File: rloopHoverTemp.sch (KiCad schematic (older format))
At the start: 23 parts, among them P1 CONN_01X01, P2 CONN_01X01, P3 CONN_01X01, P4 CONN_01X01, U1 P82B715TD, U2 MLX90614, U3 Regulator, U4 Regulator, X1 RJ45-SHIELDED, X2 RJ45-SHIELDED

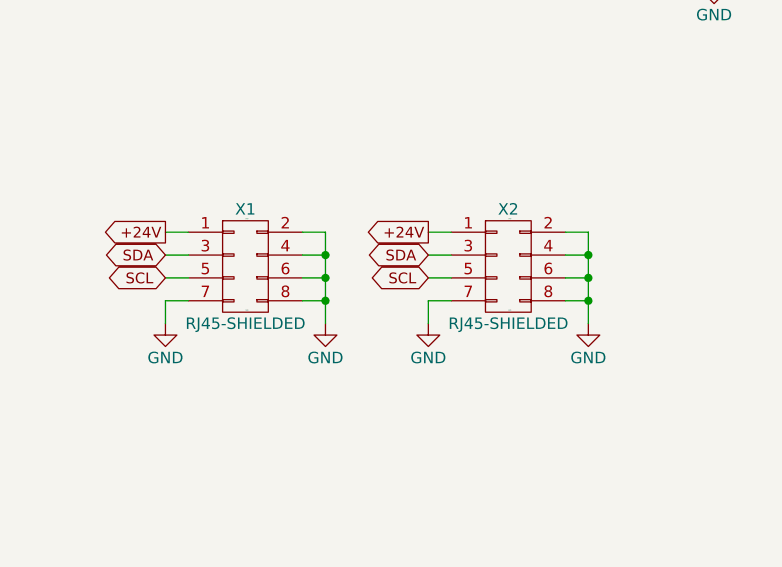
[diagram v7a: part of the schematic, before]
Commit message: different shielding scheme for RJ45
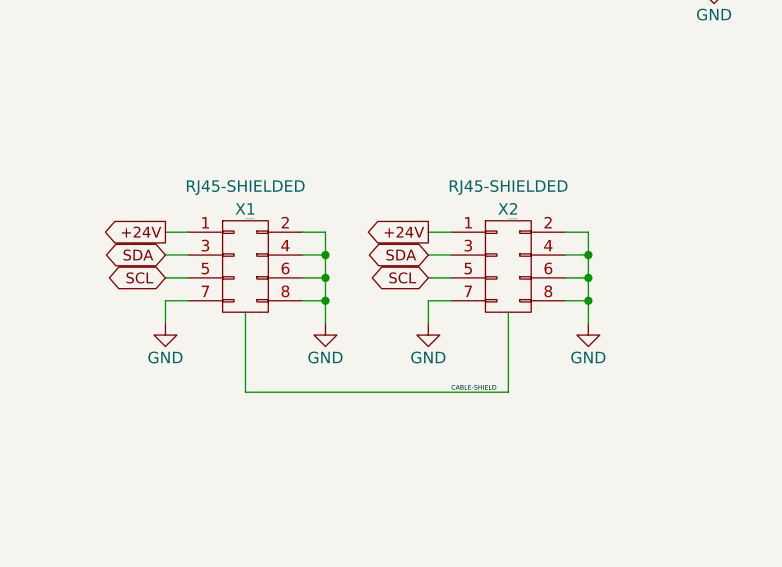
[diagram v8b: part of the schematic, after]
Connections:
- net GND: no longer X1.SHLD (SHLD2), X2.SHLD (SHLD2)
- new net CABLE-SHIELD: X1.SHLD (SHLD2), X2.SHLD (SHLD2)
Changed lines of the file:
@@
 Text GLabel 2300 3250 0    47   Output ~ 0
 +24V
-Text Label 2650 3600 0    4    ~ 0
-GND
-Text Label 2650 3200 0    4    ~ 0
-GND
 $Comp
 L RJ45-SHIELDED X1
@@
 P 2650 3400
 F 0 "X1" H 2650 3650 50  0000 C CNN
-F 1 "RJ45-SHIELDED" H 2650 3150 50  0000 C CNN
+F 1 "RJ45-SHIELDED" H 2650 3750 50  0000 C CNN
 F 2 "-footprints:RJ45-TE-5558342-1" H 2650 2200 50  0001 C CNN
 F 3 "" H 2650 2200 50  0000 C CNN
@@
 Text GLabel 3450 3250 0    47   Output ~ 0
 +24V
-Text Label 3800 3600 0    4    ~ 0
-GND
-Text Label 3800 3200 0    4    ~ 0
-GND
 $Comp
 L RJ45-SHIELDED X2
@@
 P 3800 3400
 F 0 "X2" H 3800 3650 50  0000 C CNN
-F 1 "RJ45-SHIELDED" H 3800 3150 50  0000 C CNN
+F 1 "RJ45-SHIELDED" H 3800 3750 50  0000 C CNN
 F 2 "-footprints:RJ45-TE-5558342-1" H 3800 2200 50  0001 C CNN
 F 3 "" H 3800 2200 50  0000 C CNN
@@
 	3450 3550 3450 3650
 $Comp
-L GND #PWR?
+L GND #PWR016
 U 1 1 574140D6
 P 3000 3650
-F 0 "#PWR?" H 3000 3400 50  0001 C CNN
+F 0 "#PWR016" H 3000 3400 50  0001 C CNN
 F 1 "GND" H 3000 3500 50  0000 C CNN
 F 2 "" H 3000 3650 50  0000 C CNN
@@
 $EndComp
 $Comp
-L GND #PWR?
+L GND #PWR017
 U 1 1 574141DE
 P 4150 3650
-F 0 "#PWR?" H 4150 3400 50  0001 C CNN
+F 0 "#PWR017" H 4150 3400 50  0001 C CNN
 F 1 "GND" H 4150 3500 50  0000 C CNN
 F 2 "" H 4150 3650 50  0000 C CNN
@@
 Connection ~ 3000 3350
 $Comp
-L GND #PWR?
+L GND #PWR018
 U 1 1 5741470F
 P 10200 5000
-F 0 "#PWR?" H 10200 4750 50  0001 C CNN
+F 0 "#PWR018" H 10200 4750 50  0001 C CNN
 F 1 "GND" H 10200 4850 50  0000 C CNN
 F 2 "" H 10200 5000 50  0000 C CNN
@@
 	10300 4150 10200 4150
 Connection ~ 10200 4400
+Wire Wire Line
+	2650 3600 2650 3950
+Wire Wire Line
+	2650 3950 3800 3950
+Wire Wire Line
+	3800 3950 3800 3600
+Text Label 3550 3950 0    20   ~ 0
+CABLE-SHIELD
+Text Label 3800 3200 0    4    ~ 0
+CABLE-SHIELD
+Text Label 2650 3200 0    4    ~ 0
+CABLE-SHIELD
 $EndSCHEMATC
